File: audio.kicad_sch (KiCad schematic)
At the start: 72 parts, among them U201 OPA1678, U202 OPA1678, U203 OPA1678, U204 OPA1678, U205 TAC5242, U206 OPA1678

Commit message: last stm32h7 version
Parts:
- removed R217, R218, R219, R220: 100Ω, PCM_JLCPCB:R_0805, symbol PCM_JLCPCB-Resistors:0805,100Ω
- added R217, R218, R219, R220: 100Ω, PCM_JLCPCB:R_0402, symbol PCM_JLCPCB-Resistors:0402,100Ω
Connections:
- net ADC_L+: now also C208.1; no longer C206.2
- net ADC_L-: now also C207.1; no longer C205.2
- net ADC_R+: now also C206.1; no longer C208.2
- net ADC_R-: now also C205.1; no longer C207.2
- net at R208.1, R209.1: now also U201.6 (-), U201.7; no longer U201.1, U201.2 (-)
- net at R205.1, R206.1: now also U201.1, U201.2 (-); no longer U201.6 (-), U201.7
- net at C204.1: now also C208.2, R220.2; no longer C208.1
- net at C204.2: now also C207.2, R219.2; no longer C207.1
- net at U203.6 (-), U203.7: now also R218.1
- net at U204.6 (-), U204.7: now also R220.1
- net at C203.1: now also C206.2, R218.2; no longer C206.1
- net at C203.2: now also C205.2, R217.2; no longer C205.1
- net at U204.1, U204.2 (-): now also R219.1
- net at U203.1, U203.2 (-): now also R217.1
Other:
- moved on the sheet: C203, C204, C205, C206, C207, C208, R205, R206, R207, R208, R209, R210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

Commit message: imrt1176 is added
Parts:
- removed R229, R230: 1kΩ, PCM_JLCPCB:R_1206, symbol PCM_JLCPCB-Resistors:1206,1kΩ
- added C12, C13: 47uF, PCM_JLCPCB:C_1206, symbol PCM_JLCPCB-Capacitors:1206,47uF
- added C241: 10uF, PCM_JLCPCB:C_0402, symbol PCM_JLCPCB-Capacitors:0402,10uF
- added C50, C63: 100pF, PCM_JLCPCB:C_0402, symbol PCM_JLCPCB-Capacitors:0402,100pF
- added C58: C, symbol Device:C
- added C61: ?, symbol Device:C_Polarized
- added D2, D3: BAV99, Package_TO_SOT_SMD:SOT-23, symbol Diode:BAV99
- added FB4: ?, symbol Device:FerriteBead
- added R10, R19, R20, R21, R3, R6: 10kΩ, PCM_JLCPCB:R_0402, symbol PCM_JLCPCB-Resistors:0402,10kΩ
- added R36, R39, R40, R43: 100,0.1%, Resistor_SMD:R_0805_2012Metric, symbol Device:R
- added R57: 0, symbol Device:R_Small
- added U5, U9: TL431DBZ, Package_TO_SOT_SMD:SOT-23, symbol Reference_Voltage:TL431DBZ
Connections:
- net +3.3V: now also C58.1, FB4.1; no longer U205.23 (AVDD), U205.7 (MD1), U205.8 (MD2)
- net DAC_R+: now also C232.1; no longer C231.1
- net DAC_R-: now also C231.1; no longer C232.1
- net GND: now also C12.2, C13.1, C241.2, C50.1, C58.2, C61.2, C63.1, R10.1, R39.1, R43.1, R6.2, U5.3 (A), U9.1 (K)
- net at R228.2, U206.1: now also R40.1
- net at R227.2, U206.7: now also R36.1
- net +V_OPA renamed +6.5V
- net +6.5V: now also R20.1; no longer D201.2 (A), D202.2 (A), D203.2 (A), D204.2 (A)
- net -V_OPA renamed -6.5V
- net -6.5V: now also R21.2; no longer D201.1 (K), D202.1 (K), D203.1 (K), D204.1 (K)
- net I2S_SDI renamed I2S_RX
- net I2S_SDO renamed I2S_TX
- net Line_Output_L renamed Line_Output_L+
- net Line_Output_L+: now also R40.2
- net Line_Output_R renamed Line_Output_R+
- net Line_Output_R+: now also R36.2
- new net: C241.1, FB4.2, R57.1, U205.23 (AVDD), U205.7 (MD1), U205.8 (MD2)
- new net: C61.1, R57.2
- new net: R3.2, R6.1, U5.2 (REF)
- new net: R10.2, R19.1, U9.2 (REF)
- new net +5V_Clamp: C12.1, D2.2 (A), D201.2 (A), D202.2 (A), D203.2 (A), D204.2 (A), D3.2 (A), R20.2, R3.1, U5.1 (K)
- new net -5V_Clamp: C13.2, D2.1 (K), D201.1 (K), D202.1 (K), D203.1 (K), D204.1 (K), D3.1 (K), R19.2, R21.1, U9.3 (A)
- new net Line_Output_L-: C63.2, D3.3 (K), R43.2
- new net Line_Output_R-: C50.2, D2.3 (K), R39.2
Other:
- note removed: "https://www.richtek.com/Products/Switching%20Regulators/DC_DC%20StepDown%20Convertor/RT6208?sc_lang=en&specid=RT6208"
- moved on the sheet: C209, C210, C211, C212, C213, C214, C215, C216, C217, C218, C219, C220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

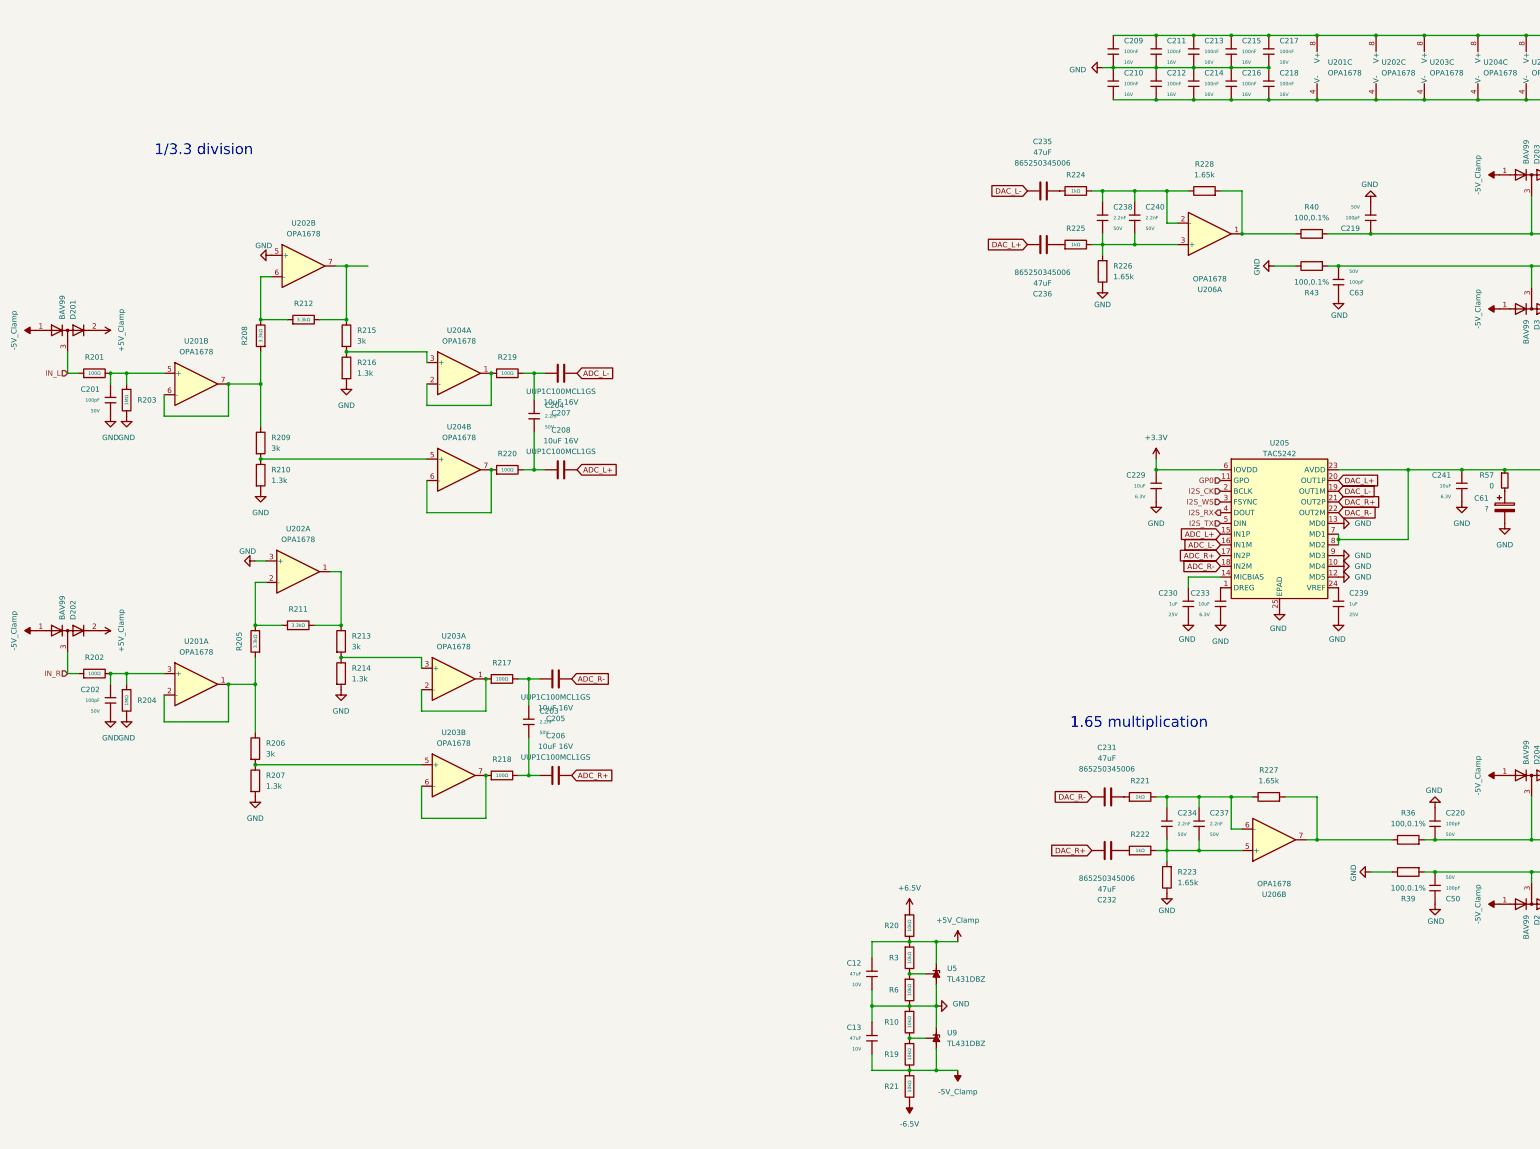
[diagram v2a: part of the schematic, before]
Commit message: added renesas RA8P1
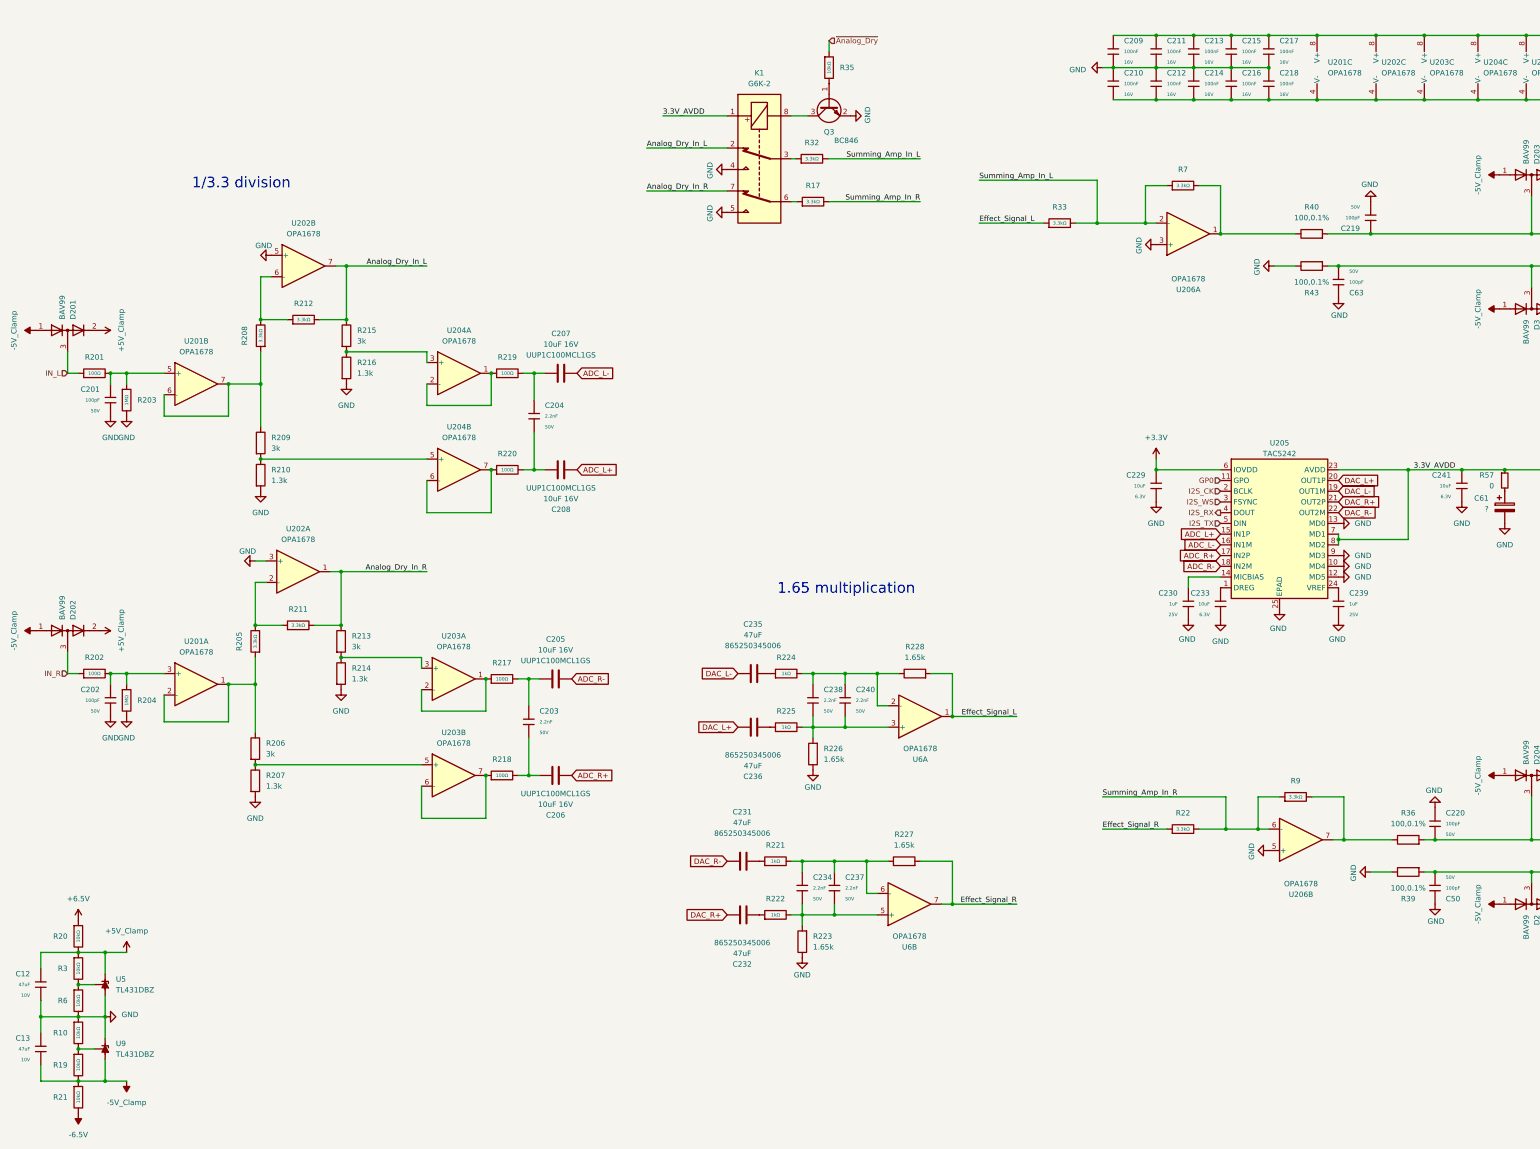
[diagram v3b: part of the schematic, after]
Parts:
- added K1: G6K-2, Relay_SMD:Relay_DPDT_Omron_G6K-2F-Y, symbol Relay:G6K-2
- added Q3: BC846, Package_TO_SOT_SMD:SOT-23, symbol Transistor_BJT:BC846
- added R17, R22, R32, R33, R7, R9: 3.3kΩ, PCM_JLCPCB:R_0402, symbol PCM_JLCPCB-Resistors:0402,3.3kΩ
- added R35: 10kΩ, PCM_JLCPCB:R_0402, symbol PCM_JLCPCB-Resistors:0402,10kΩ
- added U6: OPA1678, Package_SO:VSSOP-8_3x3mm_P0.65mm, symbol Amplifier_Operational:OPA1678
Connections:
- net GND: now also U206.3 (+), U206.5 (+), K1.4, K1.5, Q3.2 (E)
- net at C238.1, C240.1, R225.2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: now also U6.3 (+); no longer U206.3 (+)
- net at C238.2, C240.2, R224.2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: now also U6.2 (-); no longer U206.2 (-)
- net at R40.1, U206.1: now also R7.2; no longer R228.2
- net 3.3V_AVDD: now reaches C241.1, FB4.2, R57.1, U205.23 (AVDD), U205.7 (MD1), U205.8 (MD2)
- net 3.3V_AVDD: now also K1.1
- net at C234.1, C237.1, R222.2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: now also U6.5 (+); no longer U206.5 (+)
- net at C234.2, C237.2, R221.2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: now also U6.6 (-); no longer U206.6 (-)
- net at R36.1, U206.7: now also R9.2; no longer R227.2
- net Analog_Dry_In_R: now reaches R211.2, R213.1, U202.1
- net Analog_Dry_In_R: now also K1.7
- net Analog_Dry_In_L: now reaches R212.2, R215.1, U202.7
- net Analog_Dry_In_L: now also K1.2
- new net: K1.3, R32.1
- new net: Q3.1 (B), R35.2
- new net: K1.8, Q3.3 (C)
- new net: K1.6, R17.1
- new net Effect_Signal_L: R228.2, R33.1, U6.1
- new net Effect_Signal_R: R22.1, R227.2, U6.7
- new net Summing_Amp_In_L: R32.2, R33.2, R7.1, U206.2 (-)
- new net Summing_Amp_In_R: R17.2, R22.2, R9.1, U206.6 (-)
- new net ~{Analog_Dry}: R35.1
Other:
- moved on the sheet: C12, C13, C231, C232, C234, C235, C236, C237, C238, C240, R10, R19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

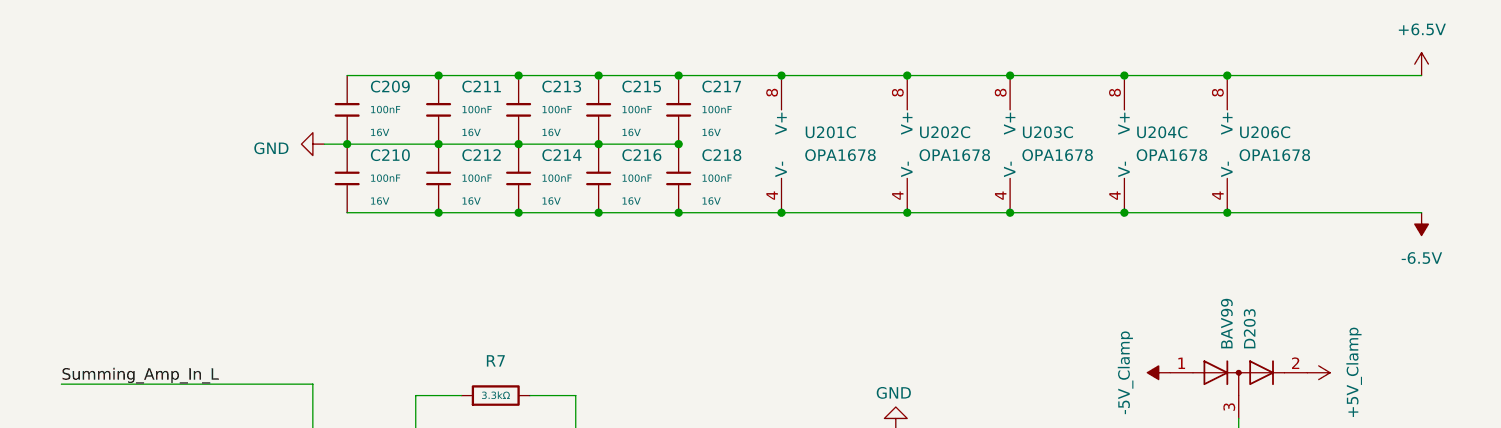
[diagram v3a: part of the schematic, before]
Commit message: progressed with SDRAM layout
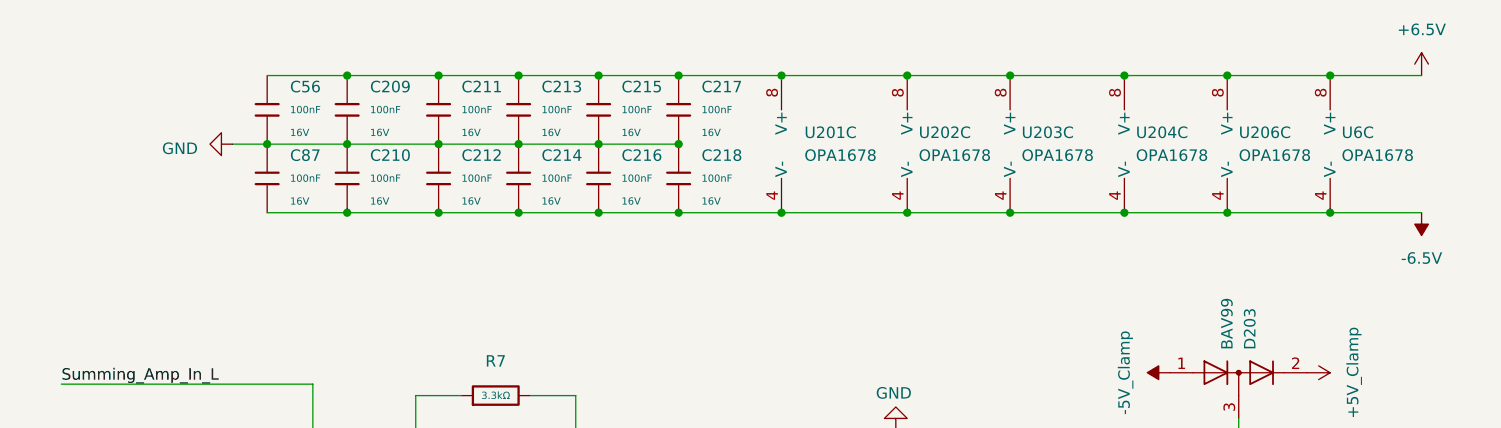
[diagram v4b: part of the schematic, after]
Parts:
- added C56, C87: 100nF, PCM_JLCPCB:C_0402, symbol PCM_JLCPCB-Capacitors:0402,100nF
- added unit 3 of U6
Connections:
- net +6.5V: now also C56.1, U6.8 (V+)
- net -6.5V: now also C87.2, U6.4 (V-)
- net GND: now also C56.2, C87.1

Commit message: layout progress
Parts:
- removed C12, C13: 47uF, PCM_JLCPCB:C_1206, symbol PCM_JLCPCB-Capacitors:1206,47uF
- removed C58: C, symbol Device:C
- removed C61: ?, symbol Device:C_Polarized
- removed D2, D201, D202, D203, D204, D3: BAV99, Package_TO_SOT_SMD:SOT-23, symbol Diode:BAV99
- removed R10, R19, R20, R21, R3, R6: 10kΩ, PCM_JLCPCB:R_0402, symbol PCM_JLCPCB-Resistors:0402,10kΩ
- removed U5, U9: TL431DBZ, Package_TO_SOT_SMD:SOT-23, symbol Reference_Voltage:TL431DBZ
- added C58: 100u, 60mR, Capacitor_Tantalum_SMD:CP_EIA-7343-31_Kemet-D, symbol Device:C_Polarized
- added D10, D2, D3, D5, D8, D9: ESD401, PCM_JLCPCB:D_DFN1006-2L, symbol PCM_JLCPCB-Diodes:TVS-Bi,H5VL10B
- added D20: 1N4148W, PCM_JLCPCB:D_SOD-123, symbol PCM_JLCPCB-Diodes:Switching,1N4148W
- added NT1: NetTie_2, NetTie:NetTie-2_SMD_Pad0.5mm, symbol Device:NetTie_2
- FB4: footprint (none) -> Inductor_SMD:L_0805_2012Metric
- R226, R228: footprint Resistor_SMD:R_0402_1005Metric -> PCM_JLCPCB:R_0402
- R57: footprint (none) -> PCM_JLCPCB:R_0402
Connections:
- net 3.3V_AVDD: now also D20.1
- net GND: now also C58.2, D10.2, D2.2, D3.2, D5.2, D8.2, D9.2, NT1.2; no longer K1.4, K1.5, R203.2, R204.2, R207.2, R210.2, R214.2, R216.2, R223.1, R226.1, R39.1, R43.1, U202.3 (+), U202.5 (+), U206.3 (+), U206.5 (+)
- net IN_L: now also D2.1
- net IN_R: now also D5.1
- net Line_Output_L+: now also D9.1
- net Line_Output_L-: now also D10.1
- net Line_Output_R+: now also D8.1
- net Line_Output_R-: now also D3.1
- net at R57.2: now also C58.1
- net at K1.8, Q3.3 (C): now also D20.2
- new net AGND: K1.4, K1.5, NT1.1, R203.2, R204.2, R207.2, R210.2, R214.2, R216.2, R223.1, R226.1, R39.1, R43.1, U202.3 (+), U202.5 (+), U206.3 (+), U206.5 (+)
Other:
- company: (none) -> KVAD
- title: (none) -> Project Y

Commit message: progressed with the layout
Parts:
- removed C231, C232, C235, C236: 47uF, Capacitor_SMD:C_Elec_6.3x7.7, symbol Device:C
- removed C58: 100u, 60mR, Capacitor_Tantalum_SMD:CP_EIA-7343-31_Kemet-D, symbol Device:C_Polarized
- removed FB4: ?, Inductor_SMD:L_0805_2012Metric, symbol Device:FerriteBead
- removed R57: 0, PCM_JLCPCB:R_0402, symbol Device:R_Small
- U6: footprint Package_SO:SOIC-8_3.9x4.9mm_P1.27mm -> Package_SO:VSSOP-8_3x3mm_P0.65mm
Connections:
- net 3.3V_AVDD is gone; now on net +3.3V: C241.1, D20.1, K1.1, U205.23 (AVDD), U205.7 (MD1), U205.8 (MD2)
- net DAC_L+: now also R225.1
- net DAC_L-: now also R224.1
- net DAC_R+: now also R222.1
- net DAC_R-: now also R221.1
